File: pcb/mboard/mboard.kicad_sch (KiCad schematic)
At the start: 13 parts, among them J1 AudioJack3_SwitchTR, U1 SD Card holder

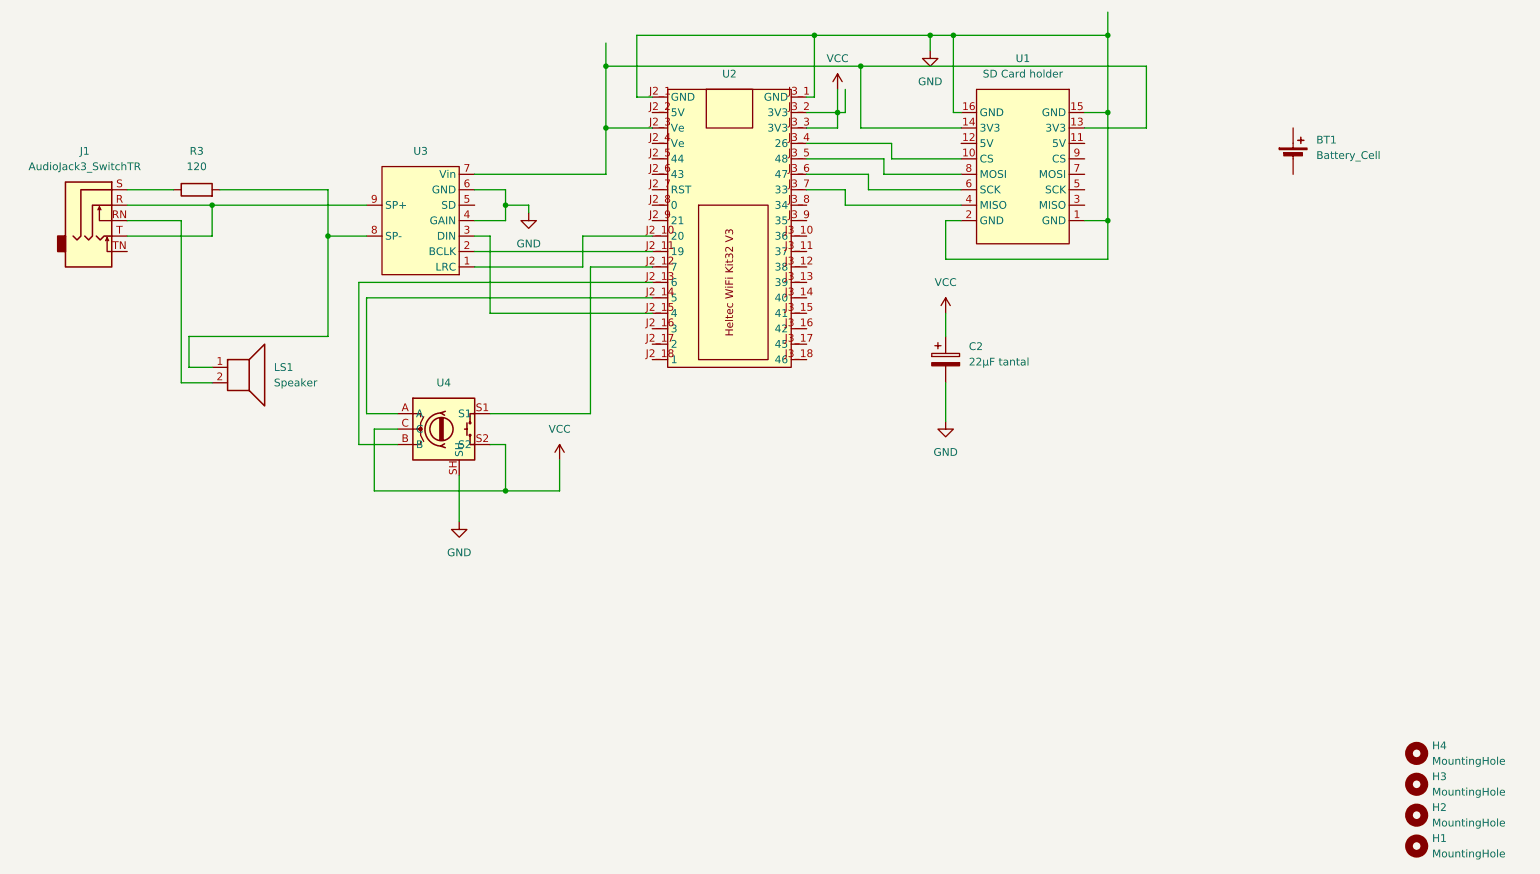
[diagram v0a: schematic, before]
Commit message: added global settings menu added new settings: screen rotation, rotary encoder speed and direction more documentation
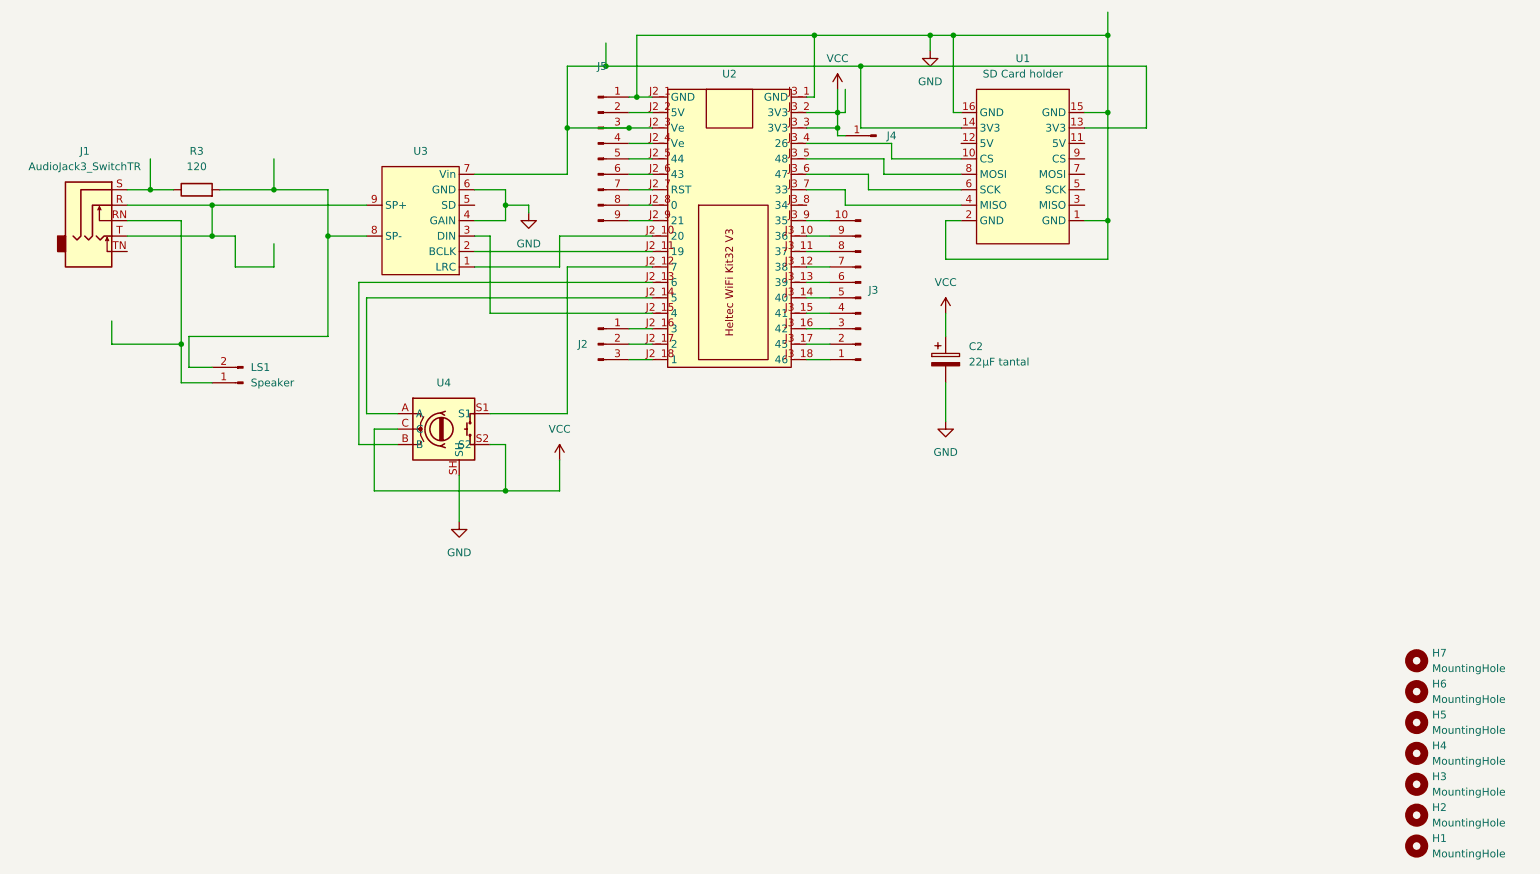
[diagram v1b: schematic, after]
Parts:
- removed BT1: Battery_Cell, Battery:BatteryHolder_MPD_BH-18650-PC2, symbol Device:Battery_Cell
- removed LS1: Speaker, components:OWS-131845W50A-8, symbol Device:Speaker
- added H5, H6, H7: MountingHole, MountingHole:MountingHole_2.7mm, symbol Mechanical:MountingHole
- added J2: Conn_01x03_Pin, Connector_PinHeader_2.54mm:PinHeader_1x03_P2.54mm_Vertical, symbol Connector:Conn_01x03_Pin
- added J3: Conn_01x10_Pin, Connector_PinHeader_2.54mm:PinHeader_1x10_P2.54mm_Vertical, symbol Connector:Conn_01x10_Pin
- added J4: Conn_01x01_Pin, Connector_PinHeader_2.54mm:PinHeader_1x01_P2.54mm_Vertical, symbol Connector:Conn_01x01_Pin
- added J5: Conn_01x09_Pin, Connector_PinHeader_2.54mm:PinHeader_1x09_P2.54mm_Vertical, symbol Connector:Conn_01x09_Pin
- added LS1: Speaker, Connector_PinHeader_2.54mm:PinHeader_1x02_P2.54mm_Vertical, symbol Connector:Conn_01x02_Pin
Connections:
- net GND: now also J5.1 (Pin_1)
- net VCC: now also J4.1 (Pin_1)
- net at U2.J2_16 (3): now also J2.1 (Pin_1)
- net at U2.J2_17 (2): now also J2.2 (Pin_2)
- net at U2.J2_18 (1): now also J2.3 (Pin_3)
- net at U2.J2_2 (5V): now also J5.2 (Pin_2)
- net at U1.13 (3V3), U1.14 (3V3), U2.J2_3 (Ve)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: now also J5.3 (Pin_3)
- net at U2.J2_4 (Ve): now also J5.4 (Pin_4)
- net at U2.J2_5 (44): now also J5.5 (Pin_5)
- net at U2.J2_6 (43): now also J5.6 (Pin_6)
- net at U2.J2_7 (RST): now also J5.7 (Pin_7)
- net at U2.J2_8 (0): now also J5.8 (Pin_8)
- net at U2.J2_9 (21): now also J5.9 (Pin_9)
- net at U2.J3_10 (36): now also J3.9 (Pin_9)
- net at U2.J3_11 (37): now also J3.8 (Pin_8)
- net at U2.J3_12 (38): now also J3.7 (Pin_7)
- net at U2.J3_13 (39): now also J3.6 (Pin_6)
- net at U2.J3_14 (40): now also J3.5 (Pin_5)
- net at U2.J3_15 (41): now also J3.4 (Pin_4)
- net at U2.J3_16 (42): now also J3.3 (Pin_3)
- net at U2.J3_17 (45): now also J3.2 (Pin_2)
- net at U2.J3_18 (46): now also J3.1 (Pin_1)
- net at U2.J3_9 (35): now also J3.10 (Pin_10)
- net at J1.RN: now also LS1.1 (Pin_1)
- net at R3.2, U3.8 (SP-): now also LS1.2 (Pin_2)
